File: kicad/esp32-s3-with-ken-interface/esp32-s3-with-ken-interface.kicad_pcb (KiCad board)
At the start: 4 copper layers, 50.8 x 81.3 mm, 38 parts, among them J1 TYPE-C-31-M-12, Q1 UMH3N, SW1 TSC015A03526A, U1 CH340C, U2 AMS1117-3.3, U3 XDZ254-2-15-W-2.5-G1, U4 ESP32-S3-WROOM-1, U5 PM254-2-15-W-8.5

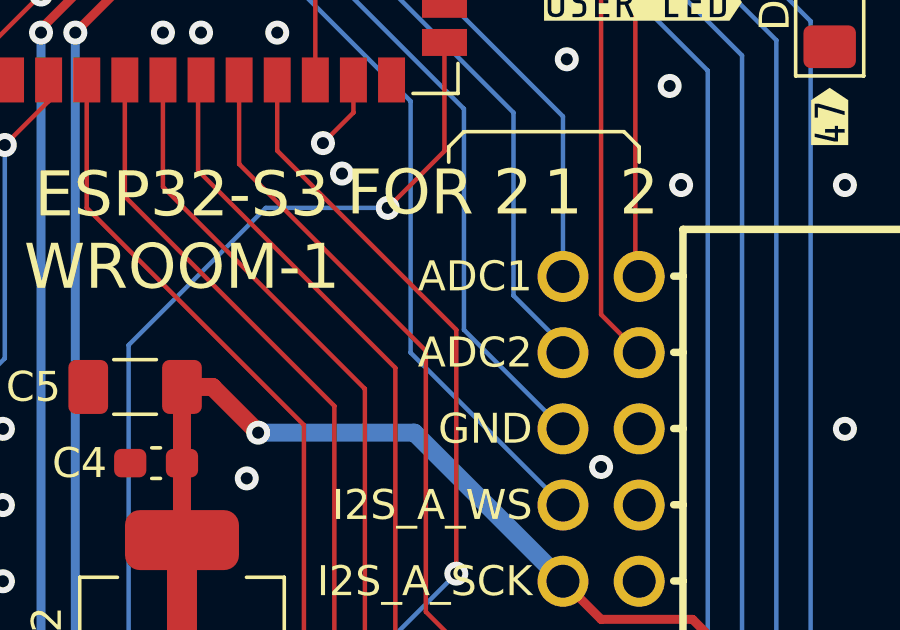
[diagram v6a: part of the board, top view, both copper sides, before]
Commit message: rename ADC_1 to ADC_A, ADC_2 to ADC_B,also update the silk text
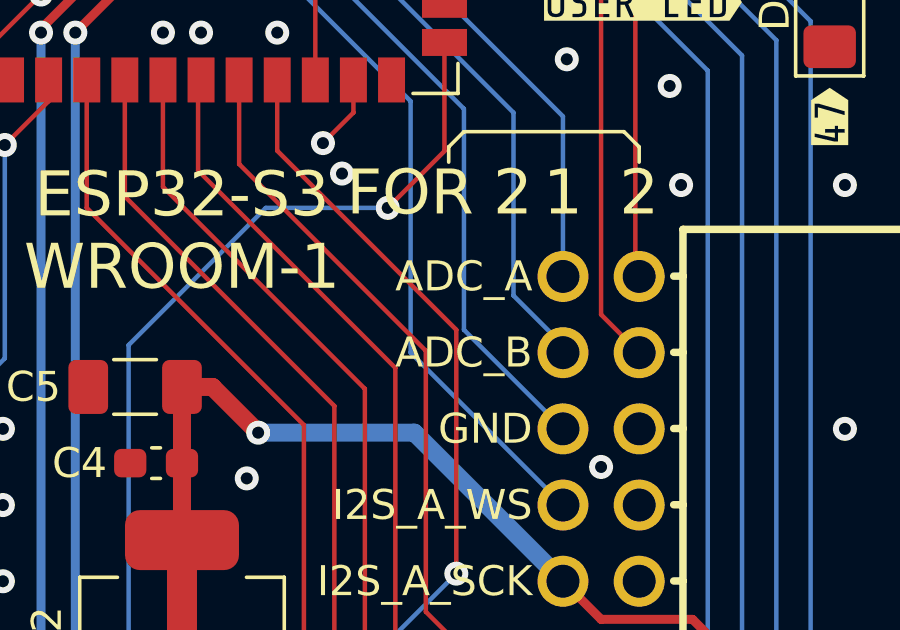
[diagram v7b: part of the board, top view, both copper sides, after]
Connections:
- net /ADC_1 renamed /ADC_A
- net /ADC_2 renamed /ADC_B
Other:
- board text added: "ADC_A"
- board text added: "ADC_B"
- board text removed: "ADC1"
- board text removed: "ADC2"
